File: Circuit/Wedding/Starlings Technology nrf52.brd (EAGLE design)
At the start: 52.4 x 52.7 mm, 22 parts, among them IC1 MCP1703CB, J7 CORTEX_DEBUG_SMD, U3 BC840M, U5 74AHCT2G125, Y2 FC-12M

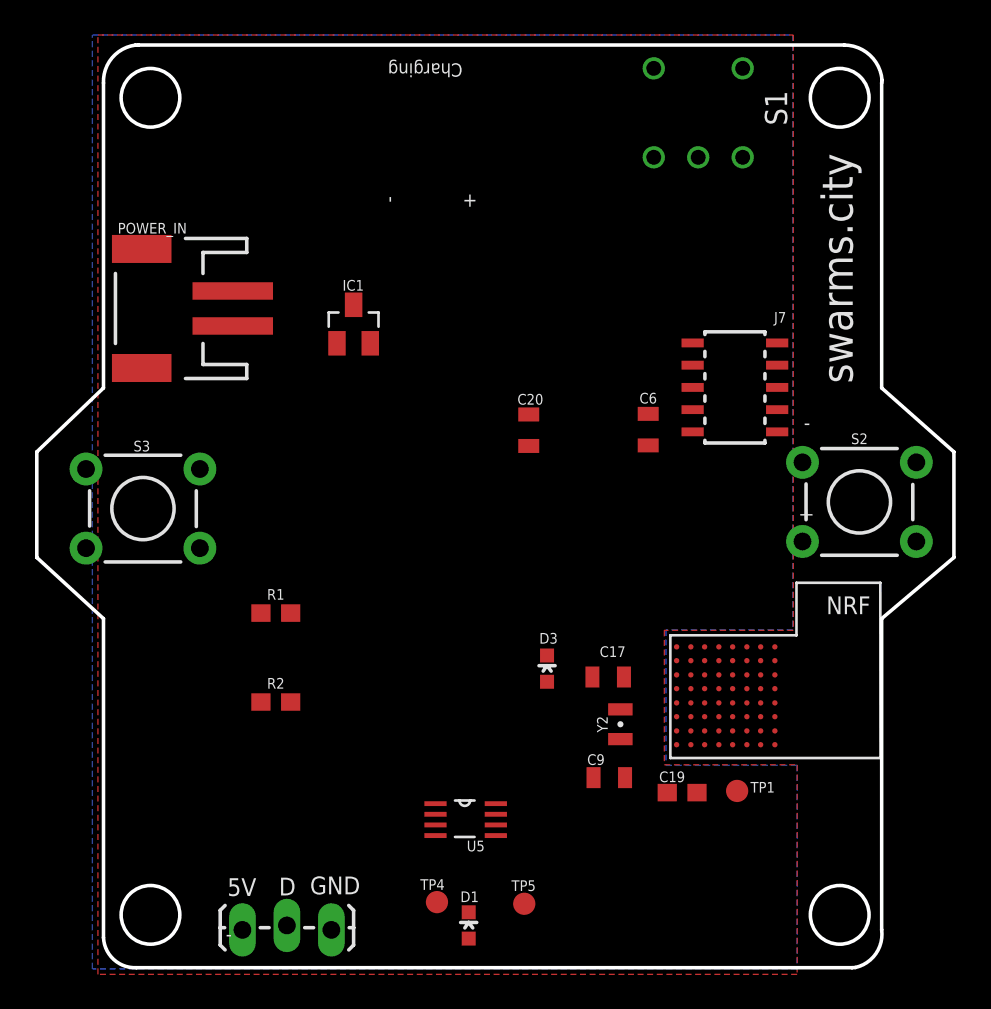
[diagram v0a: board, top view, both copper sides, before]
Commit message: Tinier size board, with new external buttons and switch.
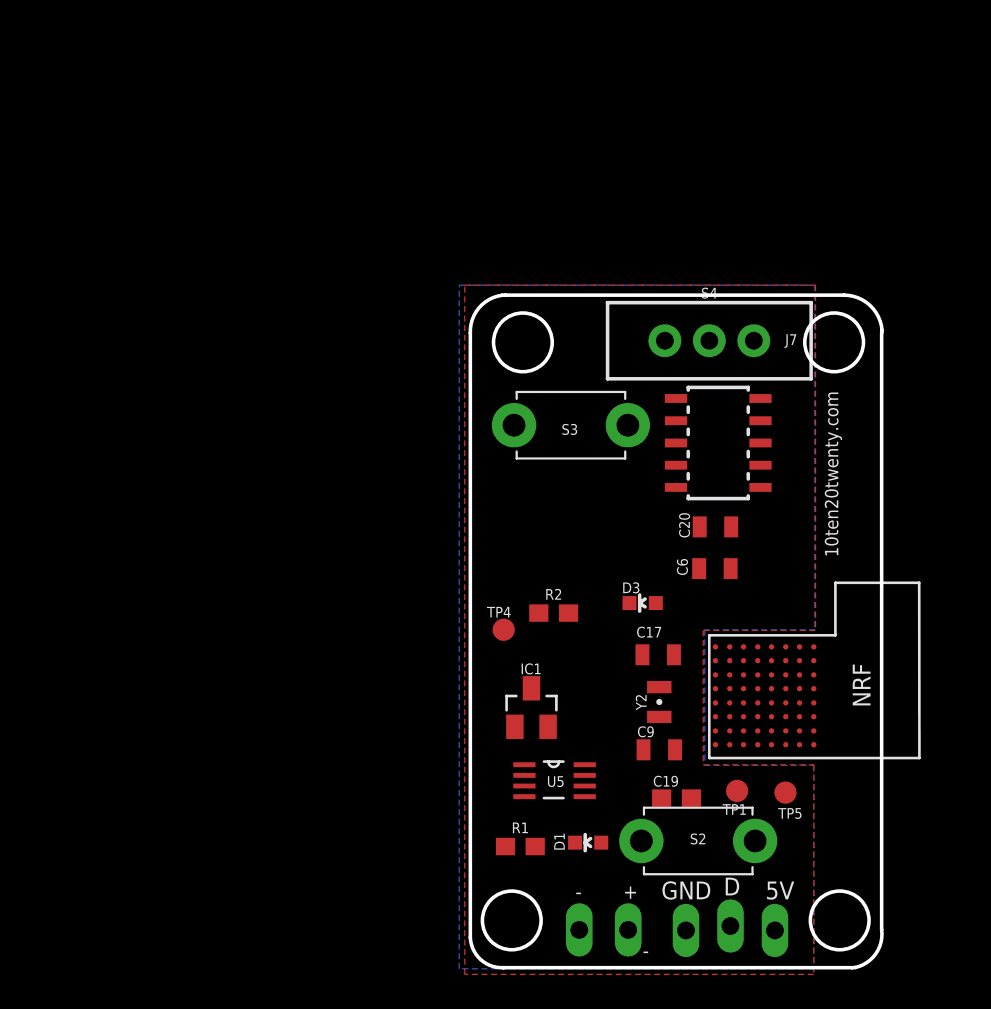
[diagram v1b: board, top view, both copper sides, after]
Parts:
- removed POWER_IN: (no value), SparkFun-Connectors:JST-2-SMD
- removed S1: CF-LD-1DC4-AR2W, RA1122DWR:CF-LD-1DC4-AR2W
- added J2: (no value), SparkFun-Connectors:1X02_LOCK_LONGPADS
- added S4: (no value), SparkFun-Switches:SWITCH_SPDT_PTH_11.6X4.0MM
- S2, S3: device SparkFun-Switches:TACTILE_SWITCH_PTH_6.0MM -> adafruit:TACT_PANA-EVQ
- moved S3 24.9 mm to (22.9, 31.4)
- moved IC1 24.1 mm to (20.6, 15.2)
- moved S2 21.4 mm to (30.2, 7.62)
- moved J1 20.3 mm to (29.5, 2.51), flipped to the bottom
- moved R1 19.3 mm to (20.0, 7.30)
- moved R2 16.7 mm to (21.9, 20.6)
- moved TP5 16.2 mm to (35.1, 10.4)
- moved TP4 16.0 mm to (19.1, 19.7)
- moved C20 12.0 mm to (31.1, 25.6), turned to 0 degrees
- moved C6 8.80 mm to (31.1, 23.2), turned to 0 degrees
- moved D1 8.31 mm to (23.9, 7.52), turned to 90 degrees
- moved D3 6.62 mm to (27.0, 21.2), turned to 90 degrees
- moved U5 5.54 mm to (21.9, 11.1)
- moved J7 3.31 mm to (31.3, 30.4)
- moved C9 3.27 mm to (27.9, 12.8)
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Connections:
- removed net 6: S1.5
- removed net N$4: C20.1, IC1.3
- net GND: now also J2.2, S2.P$1, S3.P$1; no longer POWER_IN.1, S2.1, S3.1
- net SWITCH_1: now also S3.P$2; no longer S3.3
- net SWITCH_2: now also S2.P$2; no longer S2.3
- net VBAT: now also C20.1, IC1.3, S4.1; no longer S1.3
- net VBAT_RAW: now also J2.1, S4.2; no longer POWER_IN.2, S1.4
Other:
- board size 52.4 x 52.7 mm -> 23.5 x 38.4 mm
- board text added: "10ten20twenty.com"
- board text added: "Brittany Janis + Samuel Clay"
- board text added: "Wedding Swarm Lights 10/08/2022 10ten20twenty.com"
- board text removed: "Charging"
- board text removed: "Swarm Lights V12 4/28/2022 starlings.technology"
- board text removed: "swarms.city"

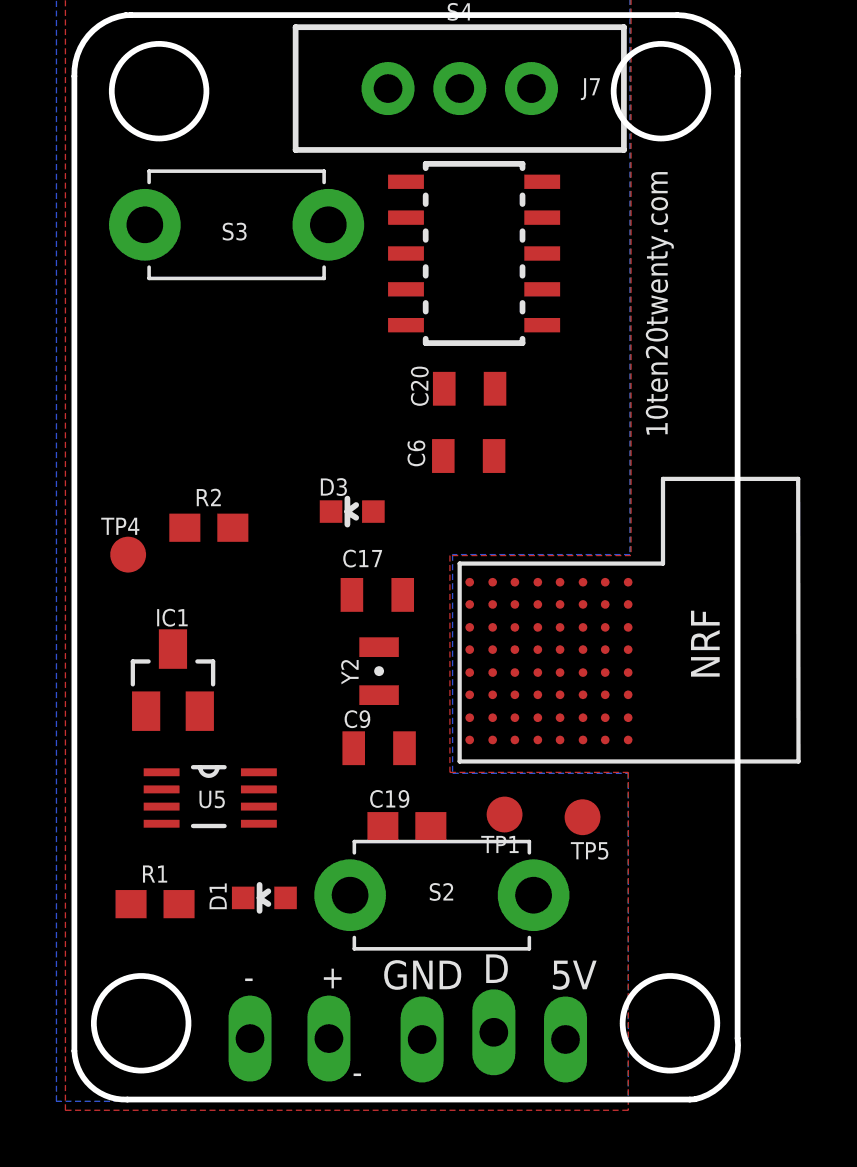
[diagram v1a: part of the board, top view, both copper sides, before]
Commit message: Moving radio in to accomodate two nrf52 module sizes.
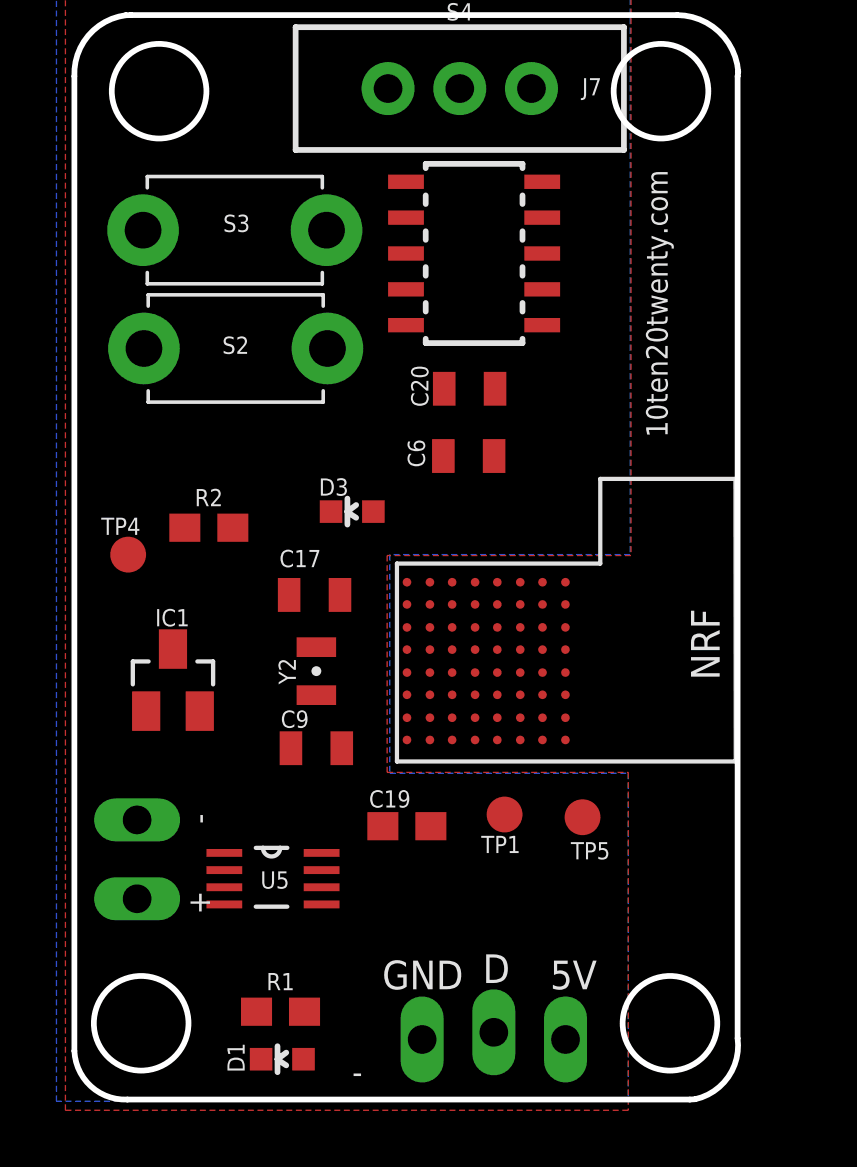
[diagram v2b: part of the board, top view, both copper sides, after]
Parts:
- moved S2 20.7 mm to (22.9, 27.0)
- moved J2 8.38 mm to (19.4, 7.62), turned to 90 degrees
- moved R1 5.85 mm to (24.4, 3.49)
- moved D1 5.75 mm to (24.5, 1.81)
- moved U5 3.62 mm to (24.1, 8.26)
- moved C17 2.22 mm to (25.7, 18.3)
- moved C9 2.22 mm to (25.7, 12.8)
- moved U3 2.22 mm to (28.6, 19.4)
- moved Y2 2.22 mm to (25.7, 15.6)
- moved S3 0.20 mm to (22.8, 31.2), turned to 0 degrees

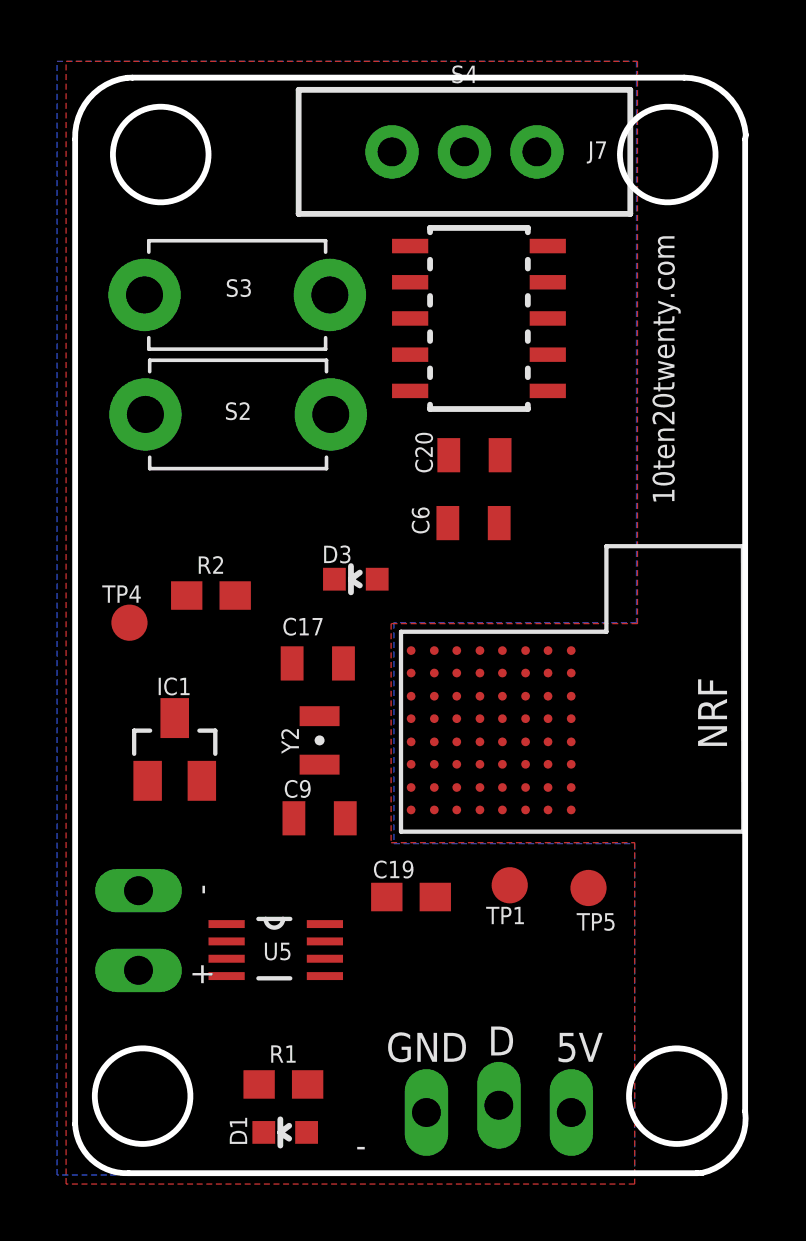
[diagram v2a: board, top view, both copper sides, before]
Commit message: Finalizing board, switched all connectors to wide pads.
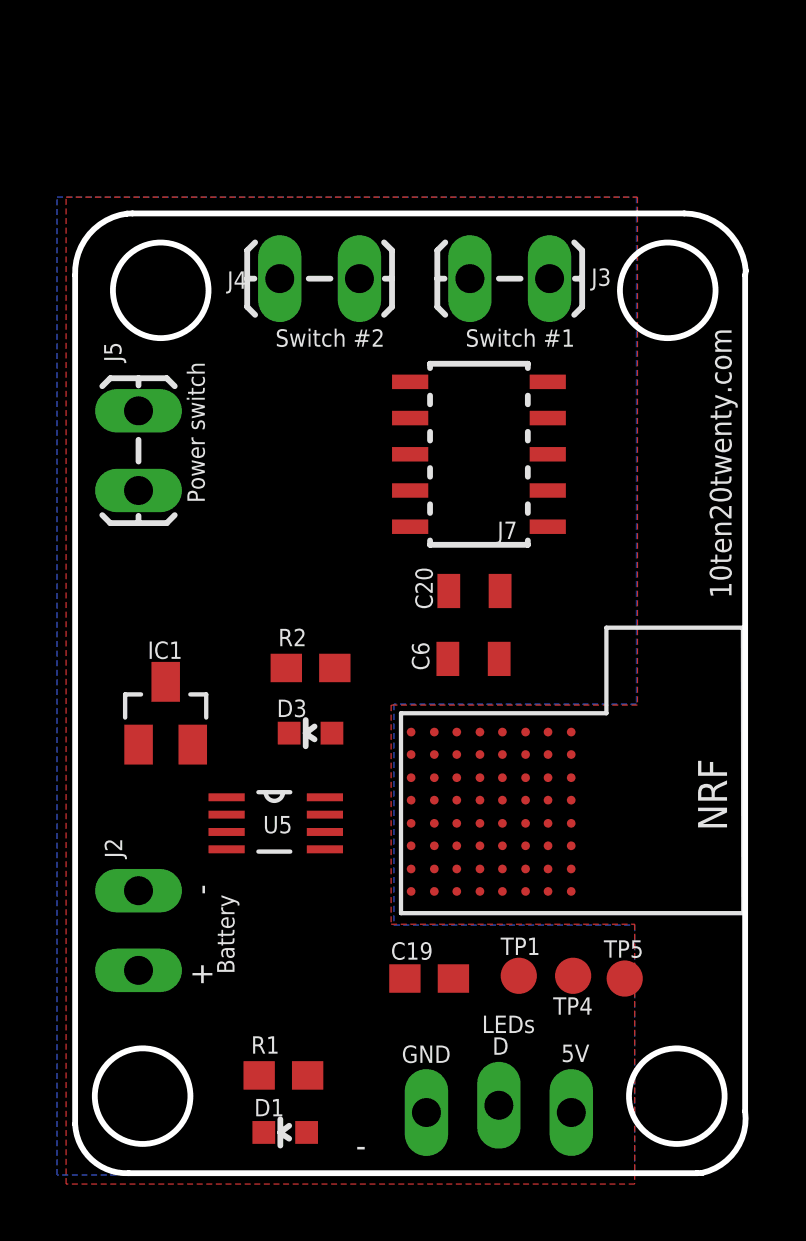
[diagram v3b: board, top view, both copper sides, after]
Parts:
- removed C17, C9: 22pF, SparkFun-Capacitors:0805
- removed S2, S3: TL1105, adafruit:TACT_PANA-EVQ
- removed S4: (no value), SparkFun-Switches:SWITCH_SPDT_PTH_11.6X4.0MM
- removed Y2: FC-12M, crystal:FC-12M
- added J3, J4, J5: (no value), SparkFun-Connectors:1X02_LOCK_LONGPADS
- moved TP4 19.9 mm to (34.6, 7.30)
- moved D3 5.63 mm to (25.4, 15.8)
- moved J7 4.76 mm to (31.3, 25.6)
- moved C20 4.76 mm to (31.1, 20.8)
- moved C6 4.76 mm to (31.1, 18.4)
- moved U5 4.44 mm to (24.1, 12.7)
- moved R2 4.32 mm to (25.4, 18.1)
- moved TP5 3.42 mm to (36.4, 7.21)
- moved TP1 3.19 mm to (32.7, 7.30)
- moved C19 2.93 mm to (29.6, 7.21)
- moved U3 2.86 mm to (28.6, 16.5)
- moved IC1 1.31 mm to (20.3, 16.5)
- moved R1 0.32 mm to (24.4, 3.81)
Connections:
- removed net N$17: C17.1, U3.F6, Y2.2
- removed net N$2: C9.1, U3.F7, Y2.1
- net GND: now also J3.1, J4.1; no longer C17.2, C9.2, S2.P$1, S3.P$1
- net SWITCH_1: now also J3.2; no longer S3.P$2
- net SWITCH_2: now also J4.2; no longer S2.P$2
- net VBAT: now also J5.1; no longer S4.1
- net VBAT_RAW: now also J5.2; no longer S4.2
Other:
- board size 23.5 x 38.4 mm -> 23.5 x 33.7 mm
- board text added: "Battery"
- board text added: "LEDs"
- board text added: "Power switch"
- board text added: "Switch #1"
- board text added: "Switch #2"

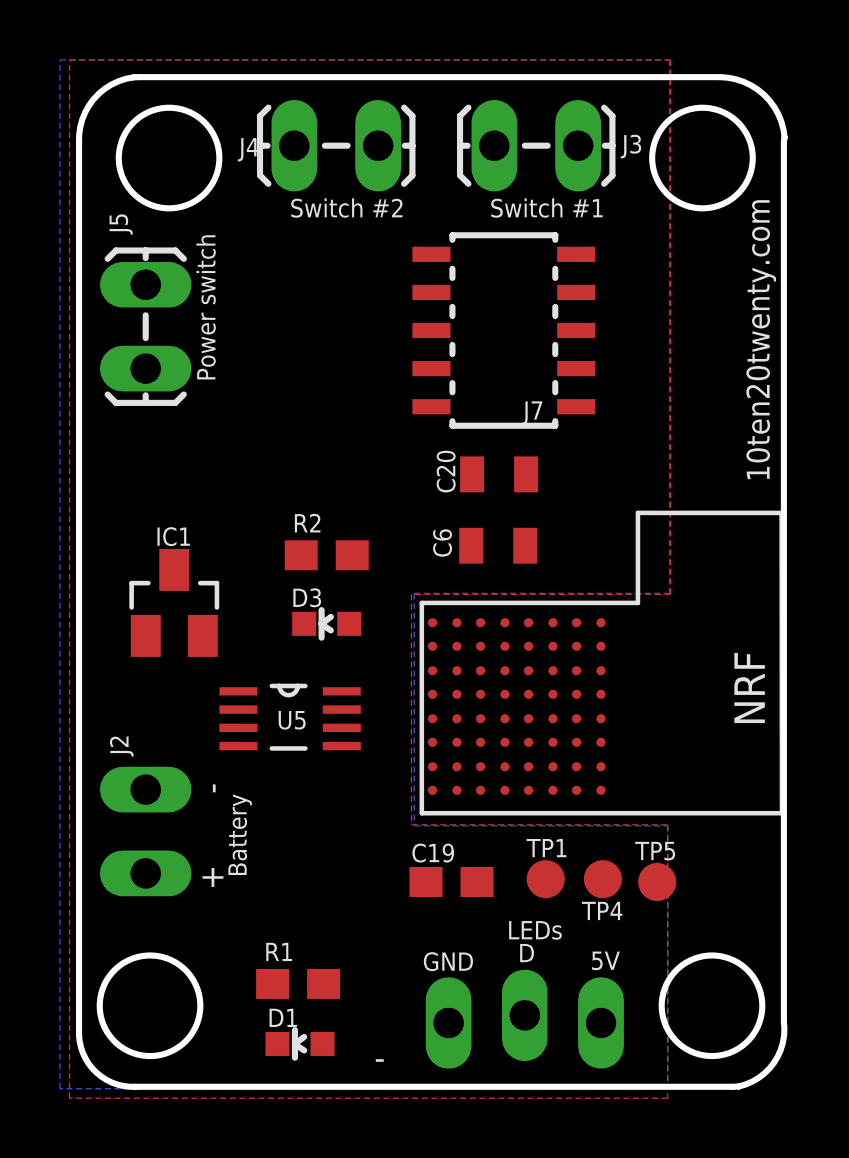
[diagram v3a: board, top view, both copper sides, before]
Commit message: Rev 2 of the wedding swarm board. Connected 5V and VBAT lines. Embiggened switches.
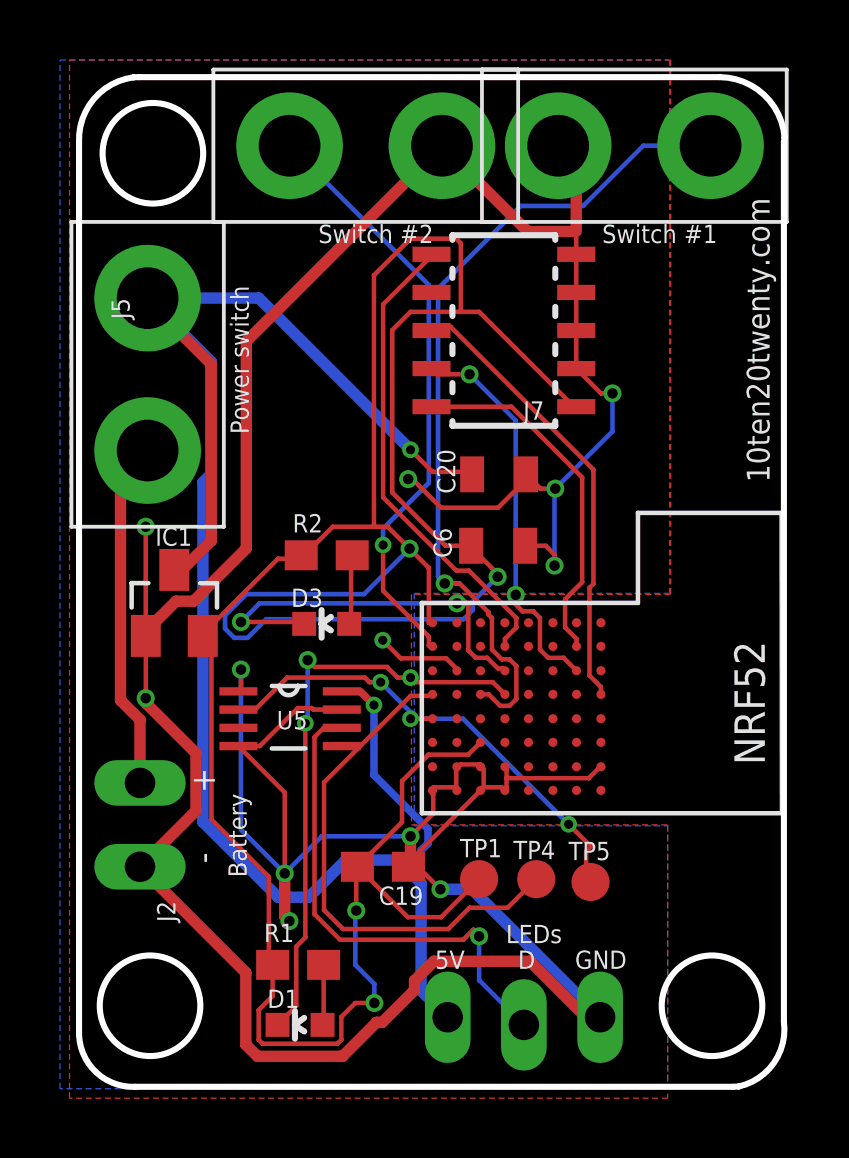
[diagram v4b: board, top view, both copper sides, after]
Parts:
- J3, J4, J5: device SparkFun-Connectors:1X02_LOCK_LONGPADS -> SparkFun-Connectors:1X02_XTRA_BIG
- moved J1 5.05 mm to (34.5, 2.70), turned to 0 degrees
- moved J3 4.54 mm to (35.7, 31.8)
- moved J5 2.86 mm to (19.4, 24.1)
- moved J2 2.77 mm to (19.2, 10.4), turned to 270 degrees
- moved C19 2.34 mm to (27.3, 7.72), turned to 0 degrees
- moved TP4 2.22 mm to (32.4, 7.30)
- moved TP5 2.22 mm to (34.2, 7.21)
- moved TP1 2.22 mm to (30.5, 7.30)
- moved R1 0.64 mm to (24.4, 4.45)
- moved D1 0.64 mm to (24.5, 2.44)
- moved J4 0.29 mm to (26.7, 31.8)
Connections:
- removed net 5V: J1.3, U5.8_VCC
- removed net PIN_01: U3.D1, U3.G1
- removed net PIN_03: U3.C7, U3.E1
- removed net PIN_04: U3.F4
- removed net SCL: U3.D6
- net PIN_02: no longer U3.E0
- net VBAT: now also J1.3, U5.8_VCC
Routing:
- net GND: track 0.00 -> 130.8 mm, vias 0 -> 11
- net 3.3V: track 0.00 -> 97.9 mm, vias 0 -> 4
- net VBAT: track 0.00 -> 64.3 mm, vias 0 -> 2
- net SWITCH_1: track 0.00 -> 27.7 mm, vias 0 -> 1
- net SWITCH_2: track 0.00 -> 20.0 mm, vias 0 -> 1
- net LED_1: track 0.00 -> 19.6 mm, vias 0 -> 3
- net HEADLAMP_3V3: track 0.00 -> 18.3 mm
- net STRIP_3V3: track 0.00 -> 16.7 mm, vias 0 -> 3
- net STRIP_5V: track 0.00 -> 16.6 mm, vias 0 -> 1
- net RESET: track 0.00 -> 16.0 mm
- net SWO: track 0.00 -> 15.1 mm
- net LED_2: track 0.00 -> 13.4 mm, vias 0 -> 2
- net SWDCLK: track 0.00 -> 13.3 mm, vias 0 -> 2
- net SWDIO: track 0.00 -> 12.0 mm
- net VBAT_RAW: track 0.00 -> 11.7 mm
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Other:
- outline, holes or cut-outs redrawn
- board text added: "NRF52"
- board text removed: "NRF"
